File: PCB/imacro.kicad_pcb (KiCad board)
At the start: 2 copper layers, 57.2 x 83.3 mm, 29 parts, among them SW0:0 Choc, SW0:1 Choc, SW0:2 Choc, SW1 TOGGLE, SW1:0 Choc, SW1:1 Choc, SW1:2 Choc, SW2:0 Choc, SW2:1 Choc, SW2:2 Choc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

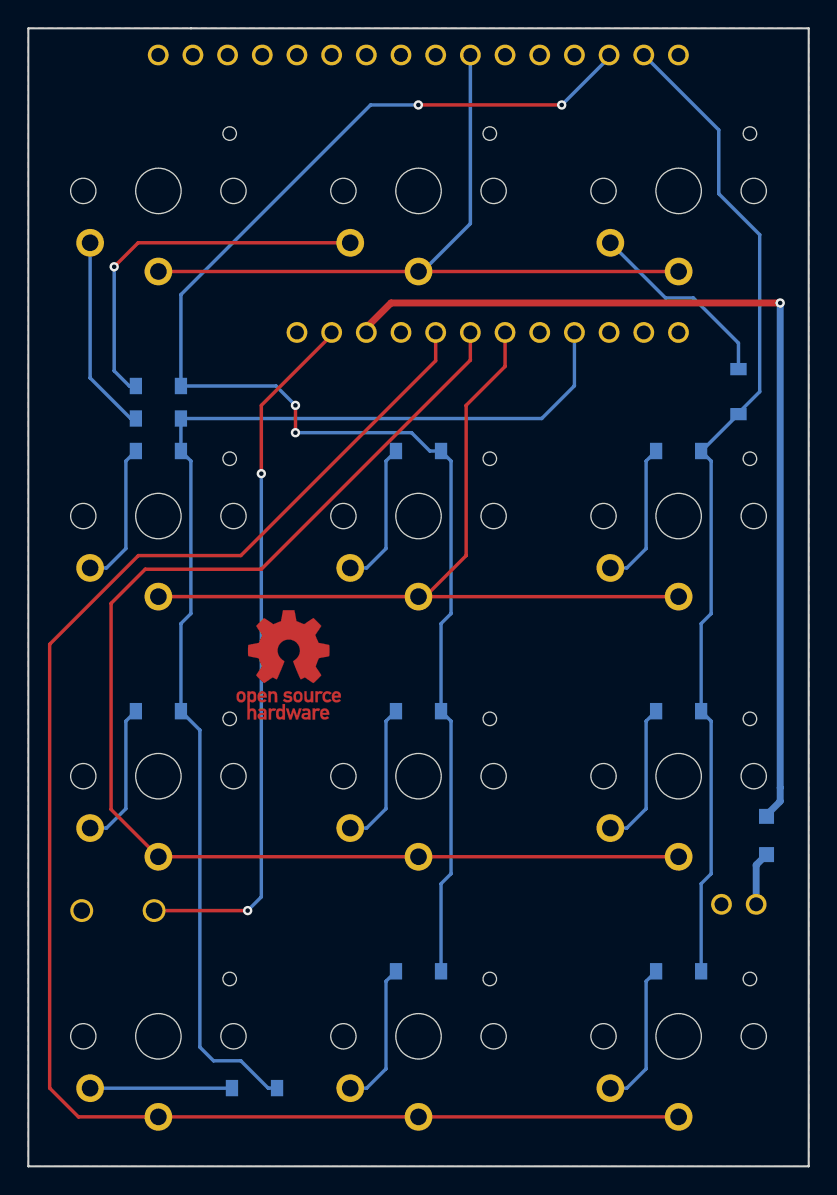
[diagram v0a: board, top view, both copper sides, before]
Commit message: Improve switch footprints (requires daprice/keyswitches.pretty ); increase annular ring size on other footprints; add positive indicator to Qi charger connection
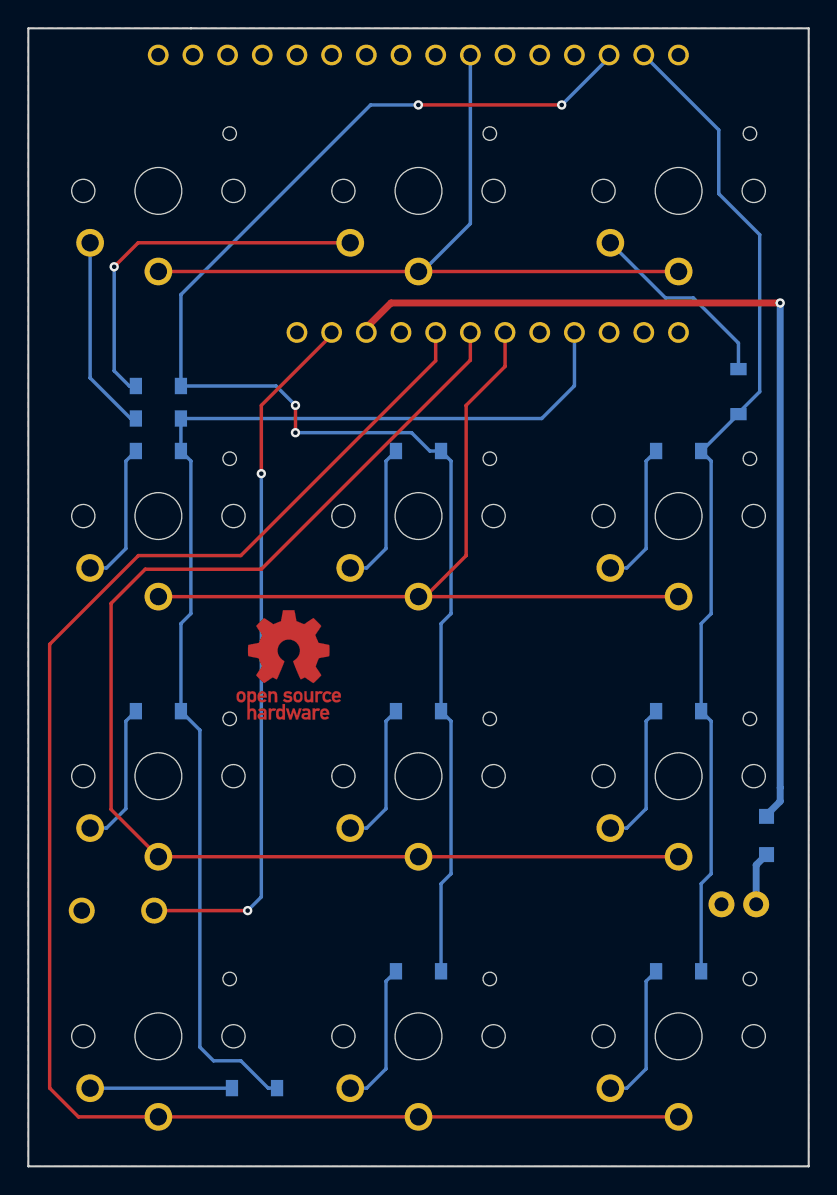
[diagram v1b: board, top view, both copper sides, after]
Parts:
- SW0:0, SW0:1, SW0:2, SW1:0, SW1:1, SW1:2, SW2:0, SW2:1, SW2:2, SW3:0, SW3:1, SW3:2: footprint imacro:PG1350 -> keyswitches:PG1350
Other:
- board text added: "+"

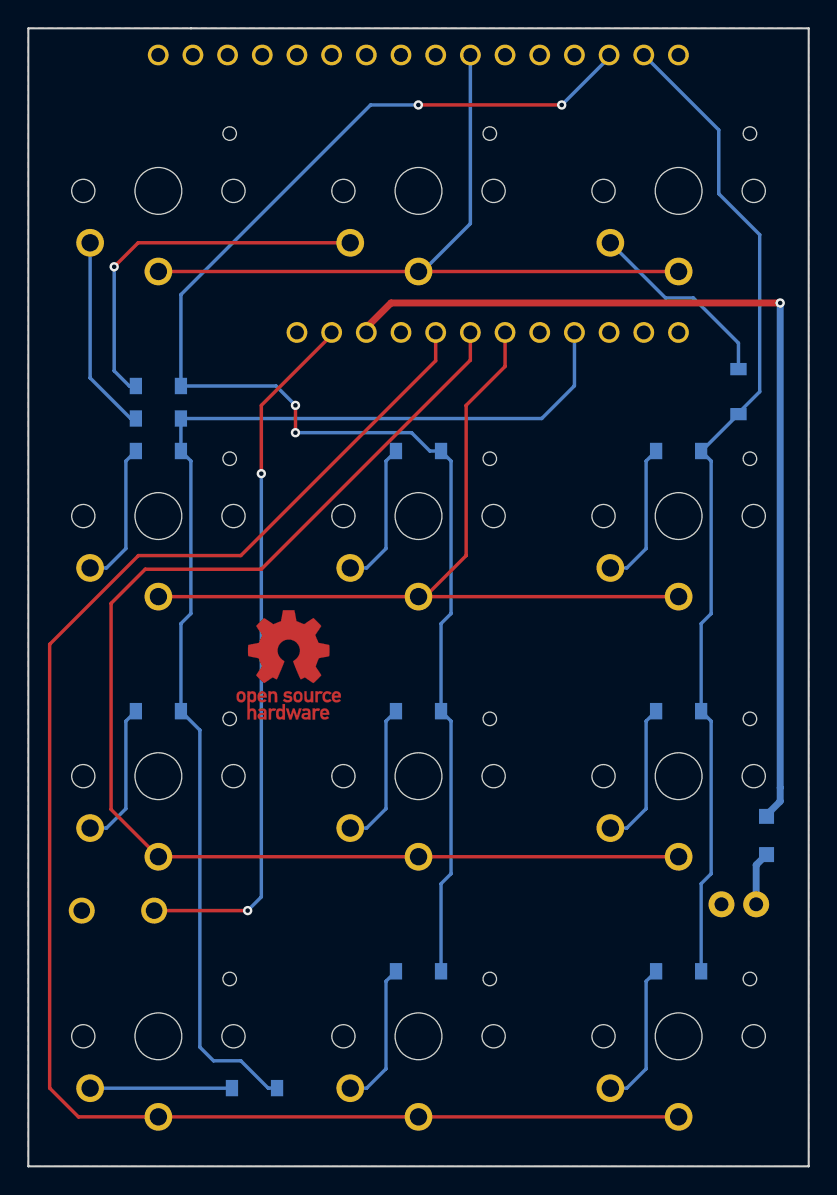
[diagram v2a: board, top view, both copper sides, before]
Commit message: Update to newer keyswitch footprint library version; update SPST pushbutton footprint to include component outline in silkscreen
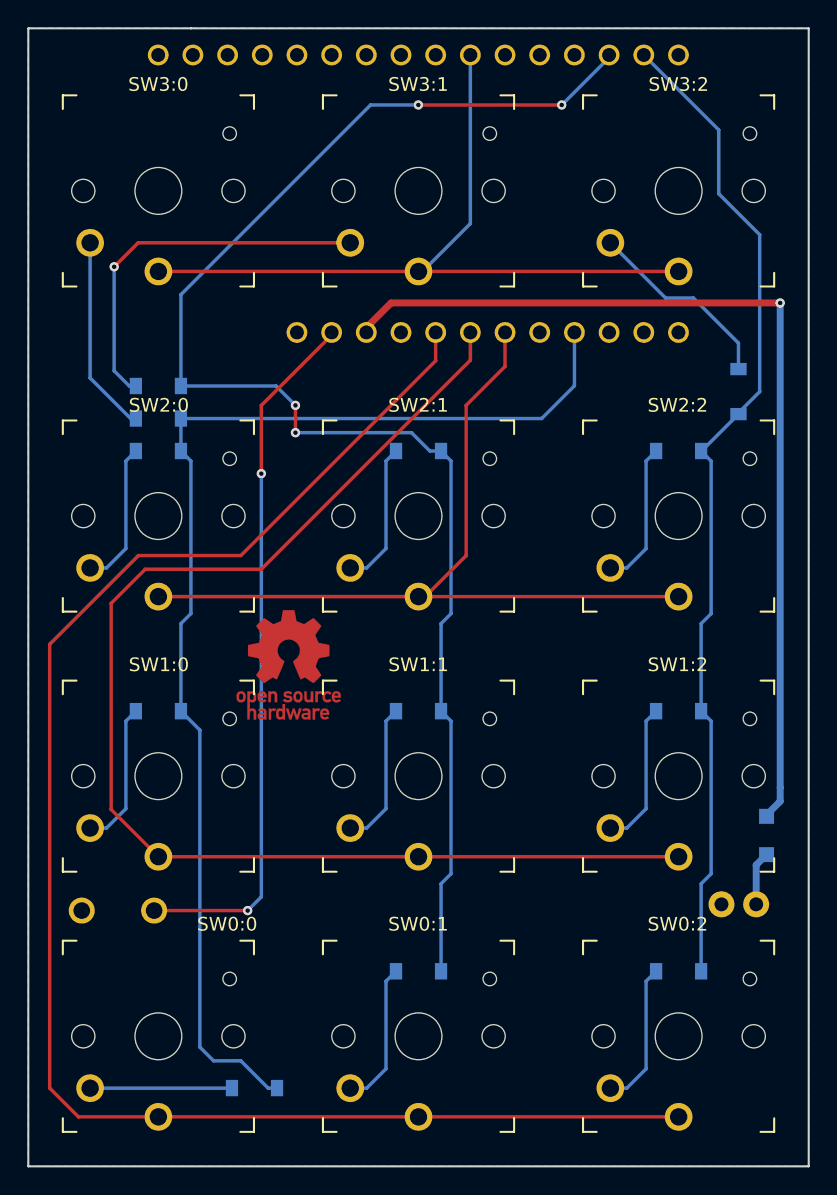
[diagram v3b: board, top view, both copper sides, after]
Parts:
- SW0:0, SW0:1, SW0:2, SW1:0, SW1:1, SW1:2, SW2:0, SW2:1, SW2:2, SW3:0, SW3:1, SW3:2: footprint keyswitches:PG1350 -> keyswitches:SW_PG1350

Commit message: Redo PCB layout with condensed (18x17mm) key spacing; adjust power button location on case to match new PCB; suffix version number on PCB with “-c” to indicate condensed variant
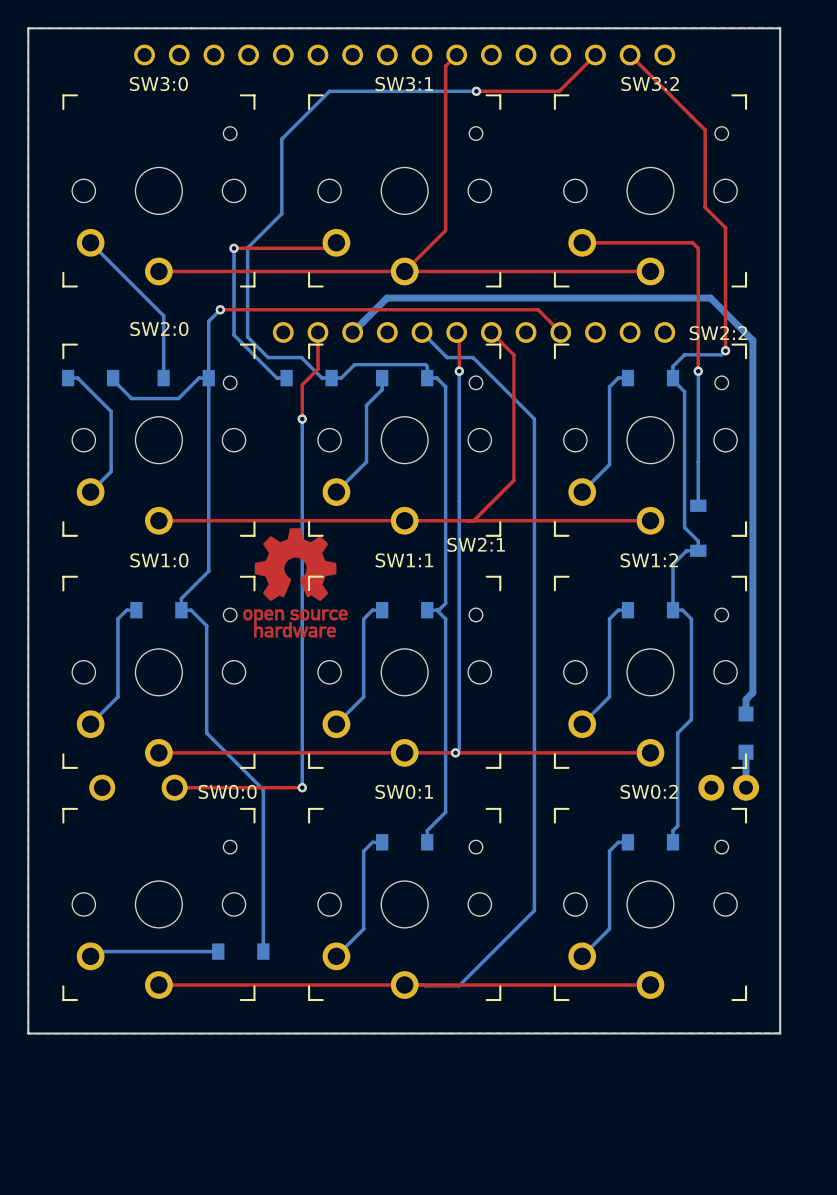
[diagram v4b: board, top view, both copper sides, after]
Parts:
- moved D3:1 11.1 mm to (92.0, 78.0)
- moved D3:2 10.4 mm to (120.5, 89.0)
- moved D0:0 10.0 mm to (87.0, 120.0)
- moved SW0:2 9.87 mm to (117.0, 116.5)
- moved SW0:1 9.71 mm to (99.0, 116.5)
- moved D0:2 9.67 mm to (117.0, 112.0)
- moved SW0:0 9.66 mm to (81.0, 116.5)
- moved D0:1 9.50 mm to (99.0, 112.0)
- moved SW1 9.12 mm to (79.5, 114.0)
- moved QI1 8.57 mm to (122.8, 108.0)
- moved SW1:2 7.88 mm to (117.0, 99.5)
- moved D1:2 7.68 mm to (117.0, 95.0)
- moved SW1:1 7.67 mm to (99.0, 99.5)
- moved D1 7.65 mm to (124.0, 104.0)
- moved SW1:0 7.61 mm to (81.0, 99.5)
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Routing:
- net /ROW1: track 94.2 -> 67.1 mm, vias 0 -> 2
- net /ROW0: track 118.4 -> 94.7 mm
- net /COL1: track 106.9 -> 93.6 mm, vias 4 -> 1
- net Net-(D3:2-Pad2): track 14.3 -> 27.5 mm, vias 0 -> 1
- net /5V_USB: track 70.0 -> 59.2 mm, vias 1 -> 0
- net Net-(SW1-Pad2): track 52.1 -> 43.2 mm
- net Net-(D3:1-Pad2): track 27.7 -> 19.2 mm
- net /ROW2: track 60.4 -> 52.2 mm
- net /COL2: track 73.6 -> 67.3 mm, vias 0 -> 1
- net /COL0: track 88.3 -> 85.0 mm, vias 0 -> 1
- net /ROW3: track 56.4 -> 53.4 mm
- net Net-(D3:0-Pad2): track 14.5 -> 12.1 mm
- net Net-(D1-Pad2): track 3.95 -> 2.60 mm
- net Net-(D0:0-Pad2): track 10.7 -> 9.49 mm
- net Net-(D2:1-Pad2): track 10.7 -> 9.74 mm
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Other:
- board size 57.2 x 83.3 mm -> 55.1 x 73.6 mm
- board text added: "v1.0-c."
- board text removed: "+"
- board text removed: "Designed for Adafruit Feather 32u4 Bluefruit"
- board text removed: "v1.0"

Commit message: Restore accidentally deleted “Designed for Adafruit Feather…” text; adjust spacing of some silkscreen elements
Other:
- board text added: "Designed for Adafruit Feather 32u4 Bluefruit LE"
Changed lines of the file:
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@@
   (general
     (thickness 1.6)
-    (drawings 8)
+    (drawings 9)
     (tracks 171)
     (zones 0)
@@
   (module imacro:QI_connector (layer B.Cu)
     (at 122.76 107.96 180)
-    (fp_text reference QI1 (at 0 2) (layer B.SilkS)
+    (fp_text reference QI1 (at 1.36 1.96) (layer B.SilkS)
       (effects (font (size 1 1) (thickness 0.15)) (justify mirror))
     )
@@
       (net 18 GND))
   )
+  (gr_text "Designed for Adafruit Feather 32u4 Bluefruit LE" (at 110 56.4) (layer B.SilkS)
+    (effects (font (size 0.738 0.738) (thickness 0.1845)) (justify mirror))
+  )
   (gr_line (start 83.34375 52.3875) (end 71.4375 52.3875) (angle 90) (layer Edge.Cuts) (width 0.15))
   (gr_line (start 83.34375 52.3875) (end 126.5 52.3875) (angle 90) (layer Edge.Cuts) (width 0.15))
@@
     (effects (font (size 0.738 0.738) (thickness 0.1845)) (justify mirror))
   )
-  (gr_text v1.0-c. (at 122 124) (layer B.SilkS)
+  (gr_text v1.0-c. (at 121.6 124.4) (layer B.SilkS)
     (effects (font (size 1.5 1.5) (thickness 0.3)) (justify mirror))
   )

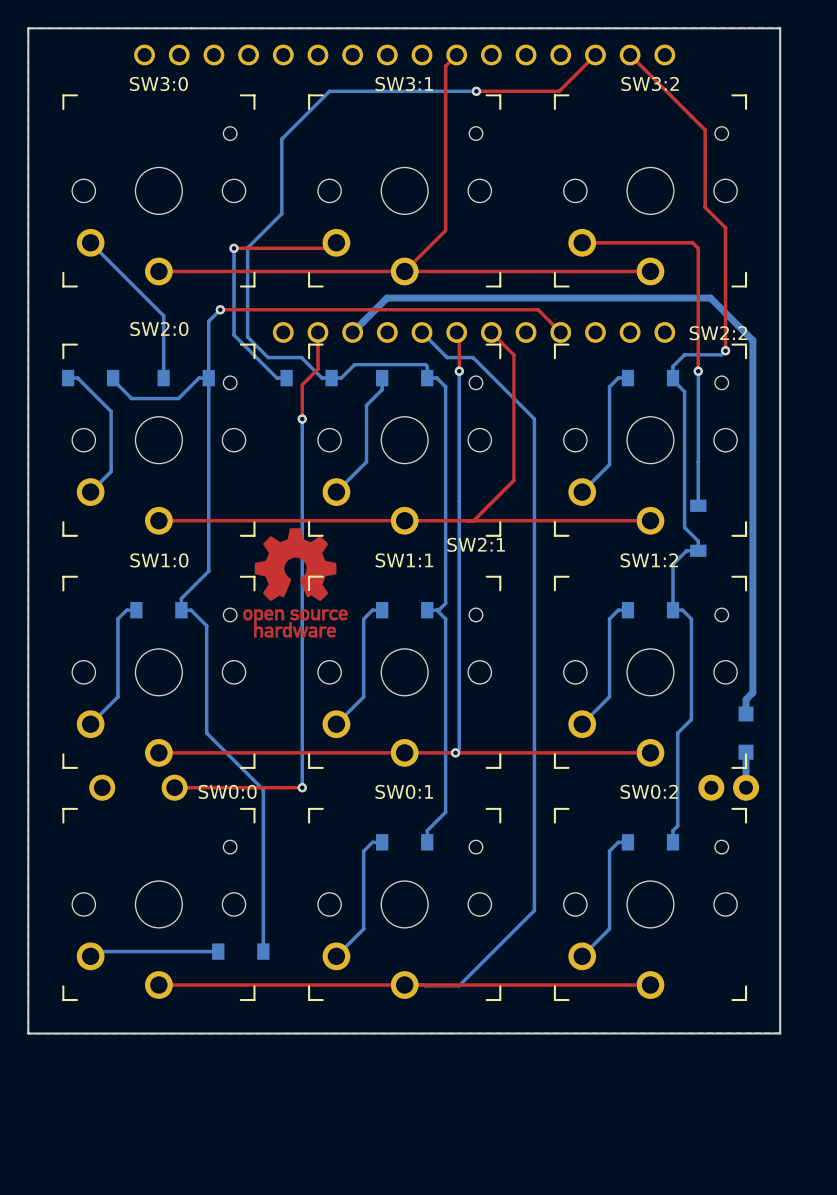
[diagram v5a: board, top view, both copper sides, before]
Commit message: Clean up some tracks and make sure vias aren’t below components
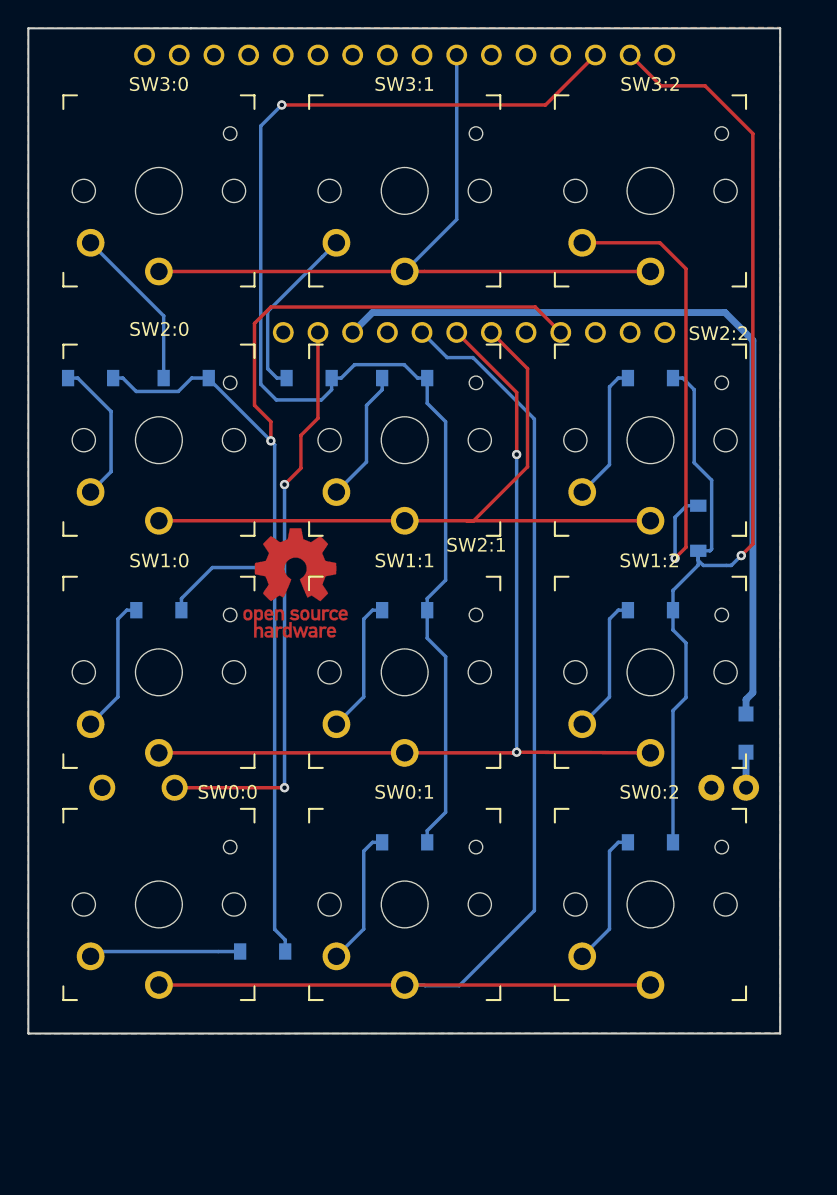
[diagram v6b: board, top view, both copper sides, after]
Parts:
- moved D0:0 1.60 mm to (88.6, 120.0)
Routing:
- net /COL2: track 67.3 -> 85.1 mm
- net /COL0: track 85.0 -> 93.7 mm
- net Net-(D3:2-Pad2): track 27.5 -> 35.0 mm
- net Net-(D3:1-Pad2): track 19.2 -> 13.6 mm, vias 1 -> 0
- net /COL1: track 93.6 -> 96.5 mm
- net /ROW1: track 67.1 -> 68.8 mm
- net Net-(D0:0-Pad2): track 9.49 -> 11.1 mm
- net /5V_USB: track 59.2 -> 58.3 mm
- net /ROW2: track 52.2 -> 53.0 mm
- net Net-(SW1-Pad2): track 43.2 -> 42.4 mm

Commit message: Update version number
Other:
- board text added: "v1.1-c."
- board text removed: "v1.0-c."
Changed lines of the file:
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@@
     (effects (font (size 0.738 0.738) (thickness 0.1845)) (justify mirror))
   )
-  (gr_text v1.0-c. (at 121.6 124.4) (layer B.SilkS)
+  (gr_text v1.1-c. (at 121.6 124.4) (layer B.SilkS)
     (effects (font (size 1.5 1.5) (thickness 0.3)) (justify mirror))
   )
